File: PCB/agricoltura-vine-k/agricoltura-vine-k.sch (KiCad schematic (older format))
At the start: 0 parts

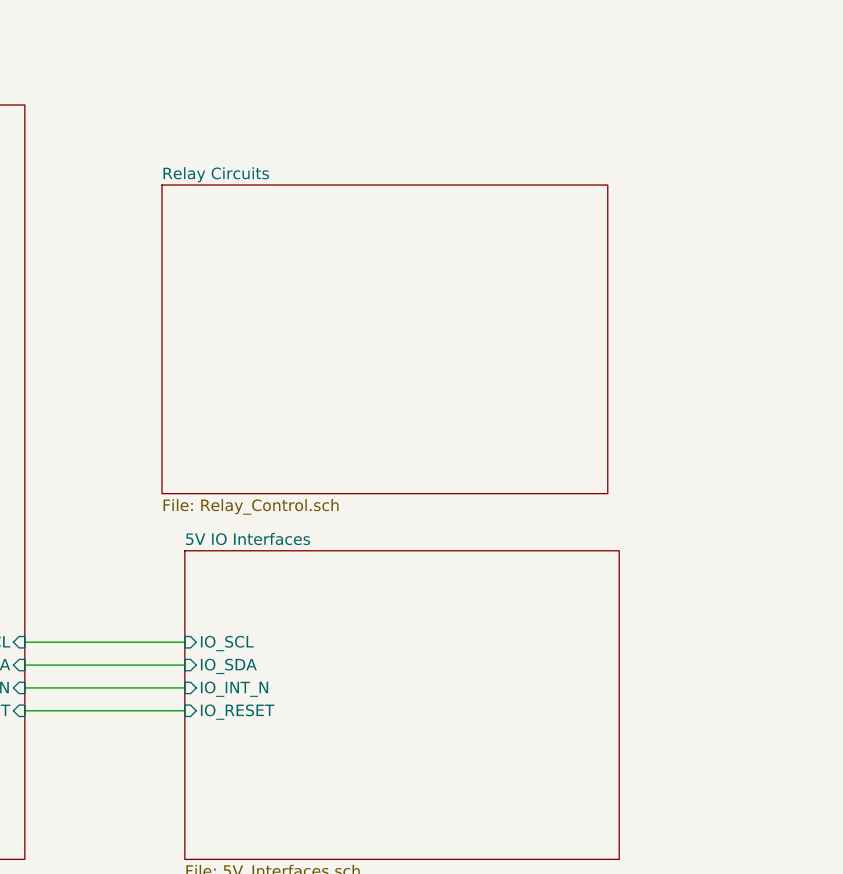
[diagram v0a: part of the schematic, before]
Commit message: Finished
PCB routing complete, up for review before fab.
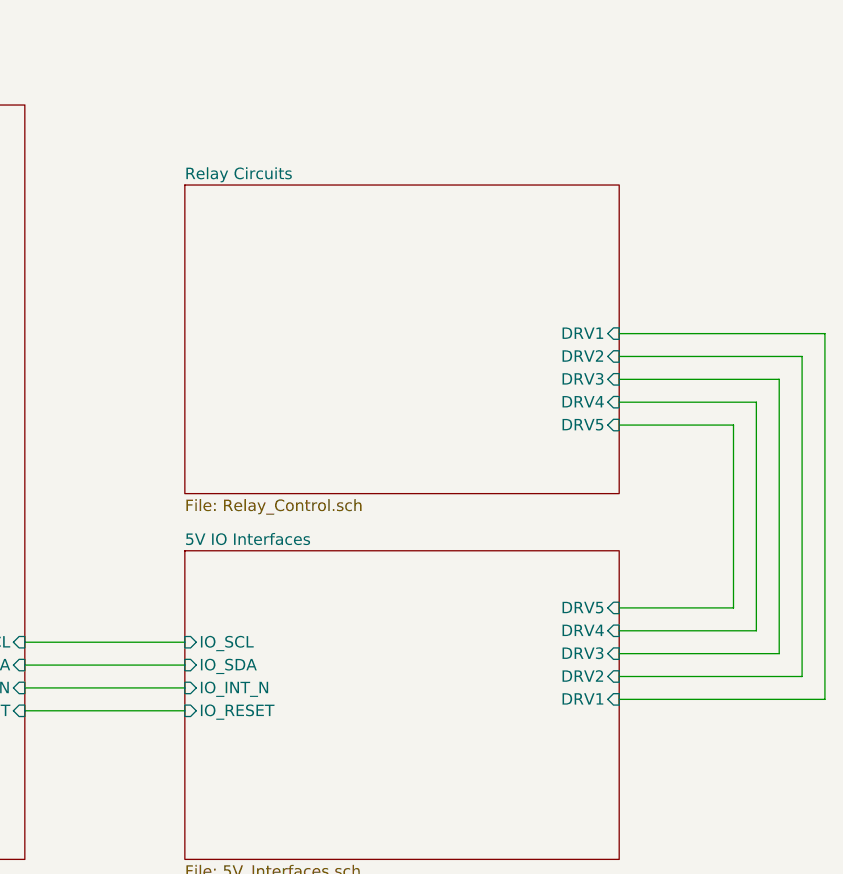
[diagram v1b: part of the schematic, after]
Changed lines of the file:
@@
 F4 "IO_INT_N" I L 7350 4550 50
 F5 "IO_RESET" I L 7350 4650 50
+F6 "DRV4" I R 9250 4300 50
+F7 "DRV3" I R 9250 4400 50
+F8 "DRV2" I R 9250 4500 50
+F9 "DRV1" I R 9250 4600 50
+F10 "DRV5" I R 9250 4200 50
 $EndSheet
 Wire Wire Line
@@
 Agricoltura Vine 0.1a
 $Sheet
-S 7250 2350 1950 1350
+S 7350 2350 1900 1350
 U 5F0125AE
 F0 "Relay Circuits" 50
 F1 "Relay_Control.sch" 50
+F2 "DRV1" I R 9250 3000 50
+F3 "DRV2" I R 9250 3100 50
+F4 "DRV3" I R 9250 3200 50
+F5 "DRV4" I R 9250 3300 50
+F6 "DRV5" I R 9250 3400 50
 $EndSheet
+Wire Wire Line
+	9250 3400 9750 3400
+Wire Wire Line
+	9750 3400 9750 4200
+Wire Wire Line
+	9750 4200 9250 4200
+Wire Wire Line
+	9250 3300 9850 3300
+Wire Wire Line
+	9850 3300 9850 4300
+Wire Wire Line
+	9850 4300 9250 4300
+Wire Wire Line
+	9250 4400 9950 4400
+Wire Wire Line
+	9950 4400 9950 3200
+Wire Wire Line
+	9950 3200 9250 3200
+Wire Wire Line
+	9250 3100 10050 3100
+Wire Wire Line
+	10050 3100 10050 4500
+Wire Wire Line
+	10050 4500 9250 4500
+Wire Wire Line
+	9250 4600 10150 4600
+Wire Wire Line
+	10150 4600 10150 3000
+Wire Wire Line
+	10150 3000 9250 3000
 $EndSCHEMATC
